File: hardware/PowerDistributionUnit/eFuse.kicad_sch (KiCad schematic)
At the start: 19 parts, among them Q2 NMOS, U1 TPS25983, U2 AD5258

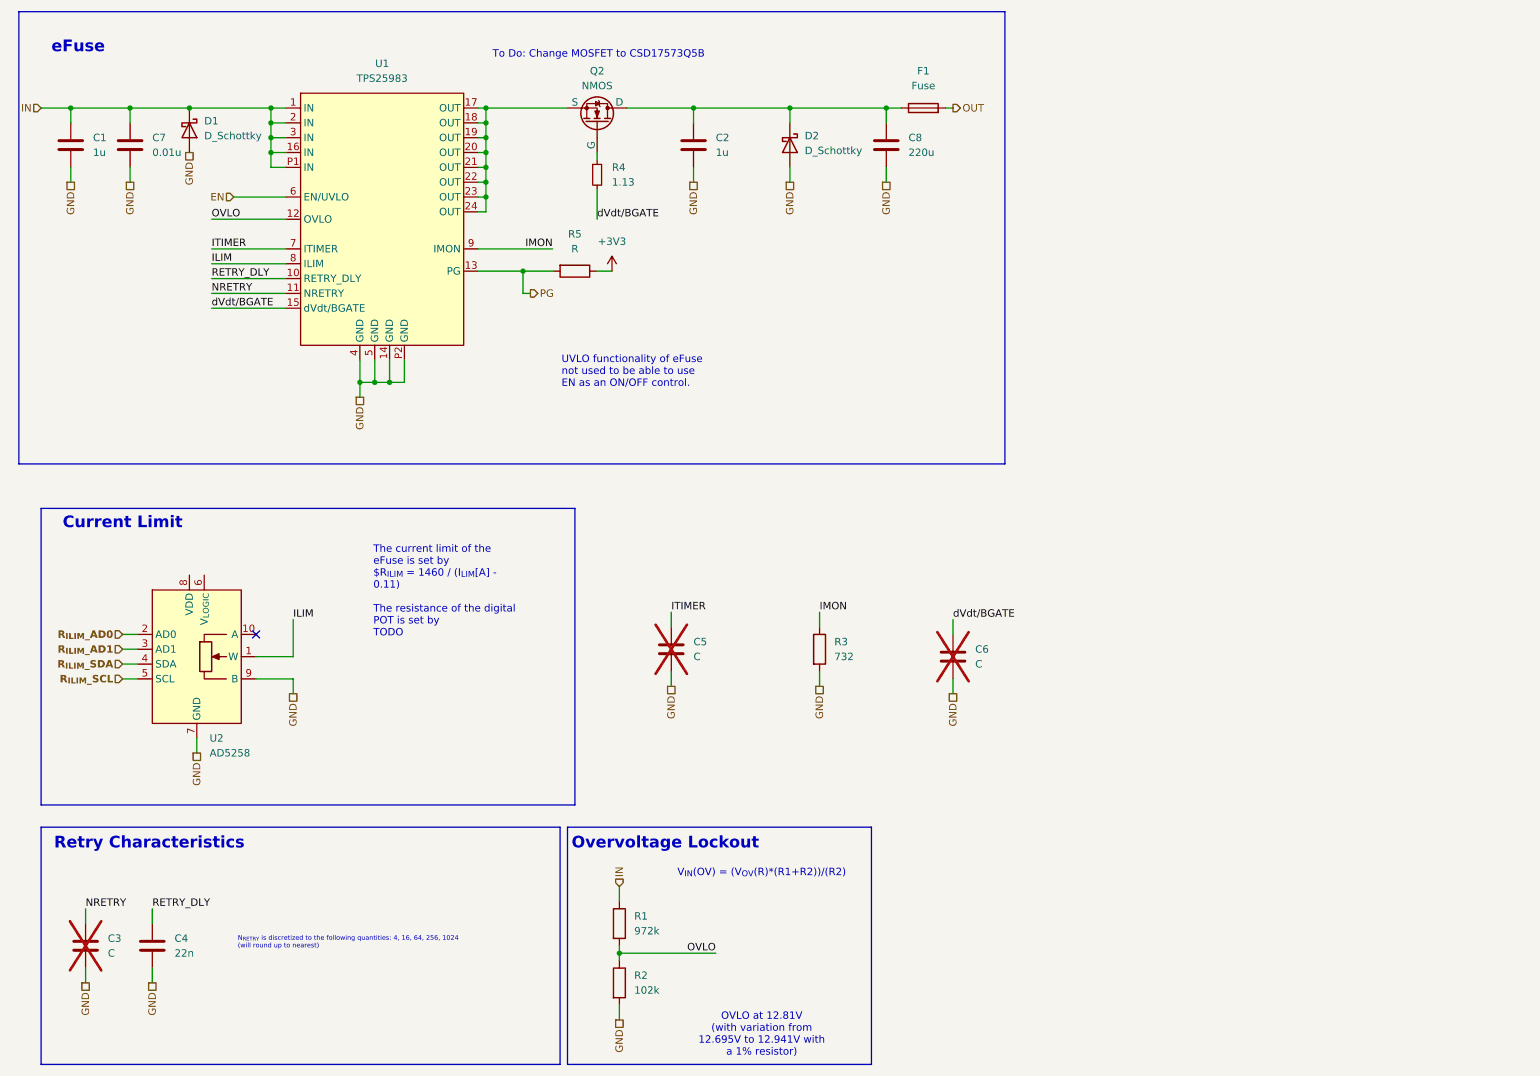
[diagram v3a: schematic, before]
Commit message: updated rev-i mosfet, organized parts, rearranged pins on digital pot symbol, added bypass caps, some rearranging, etc.
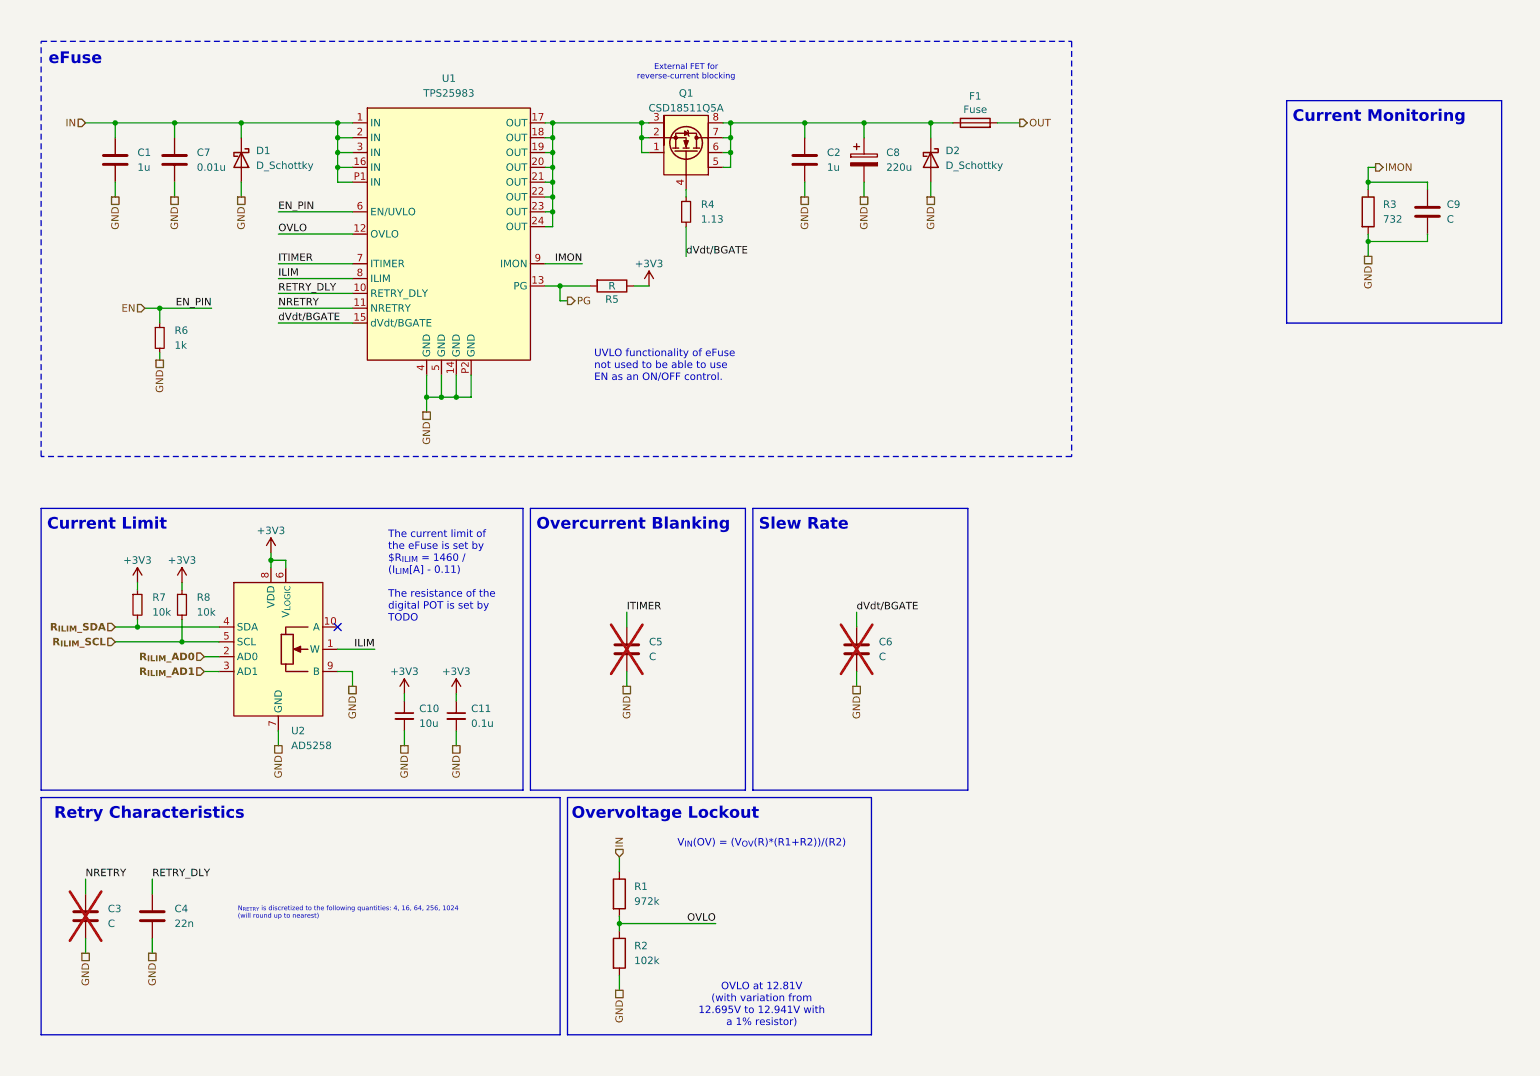
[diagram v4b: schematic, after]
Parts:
- removed C8: 220u, symbol Device:C
- removed Q2: NMOS, symbol Simulation_SPICE:NMOS
- added C10: 10u, symbol Device:C_Small
- added C11: 0.1u, symbol Device:C_Small
- added C8: 220u, symbol Device:C_Polarized
- added C9: C, symbol Device:C
- added Q1: CSD18511Q5A, symbol PowerDistributionUnitLib:CSD18511Q5A
- added R6: 1k, symbol Device:R_Small
- added R7, R8: 10k, symbol Device:R_Small
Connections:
- net +3V3: now also U2.6 (V_{LOGIC}), U2.8 (VDD), C10.1, C11.1, R7.1, R8.1
- net EN: now also R6.1
- net GND: now also C10.2, C11.2, C8.2, C9.2, R6.2
- net IMON: now also C9.1
- net R_{ILIM}_SCL: now also R8.2
- net R_{ILIM}_SDA: now also R7.2
- net at R4.1: now also Q1.4
- net at C2.1, D2.1 (K), F1.1: now also C8.1, Q1.5, Q1.6, Q1.7, Q1.8
- net at U1.17 (OUT), U1.18 (OUT), U1.19 (OUT)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: now also Q1.1, Q1.2, Q1.3
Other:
- note added: "Current Monitoring"
- note added: "Overcurrent Blanking"
- note added: "Slew Rate"
- note removed: "To Do: Change MOSFET to CSD17573Q5B"
- moved on the sheet: C1, C2, C3, C4, C5, C6, C7, D1, D2, F1, R1, R2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

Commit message: Finished eFuse schematic and now connecting everything
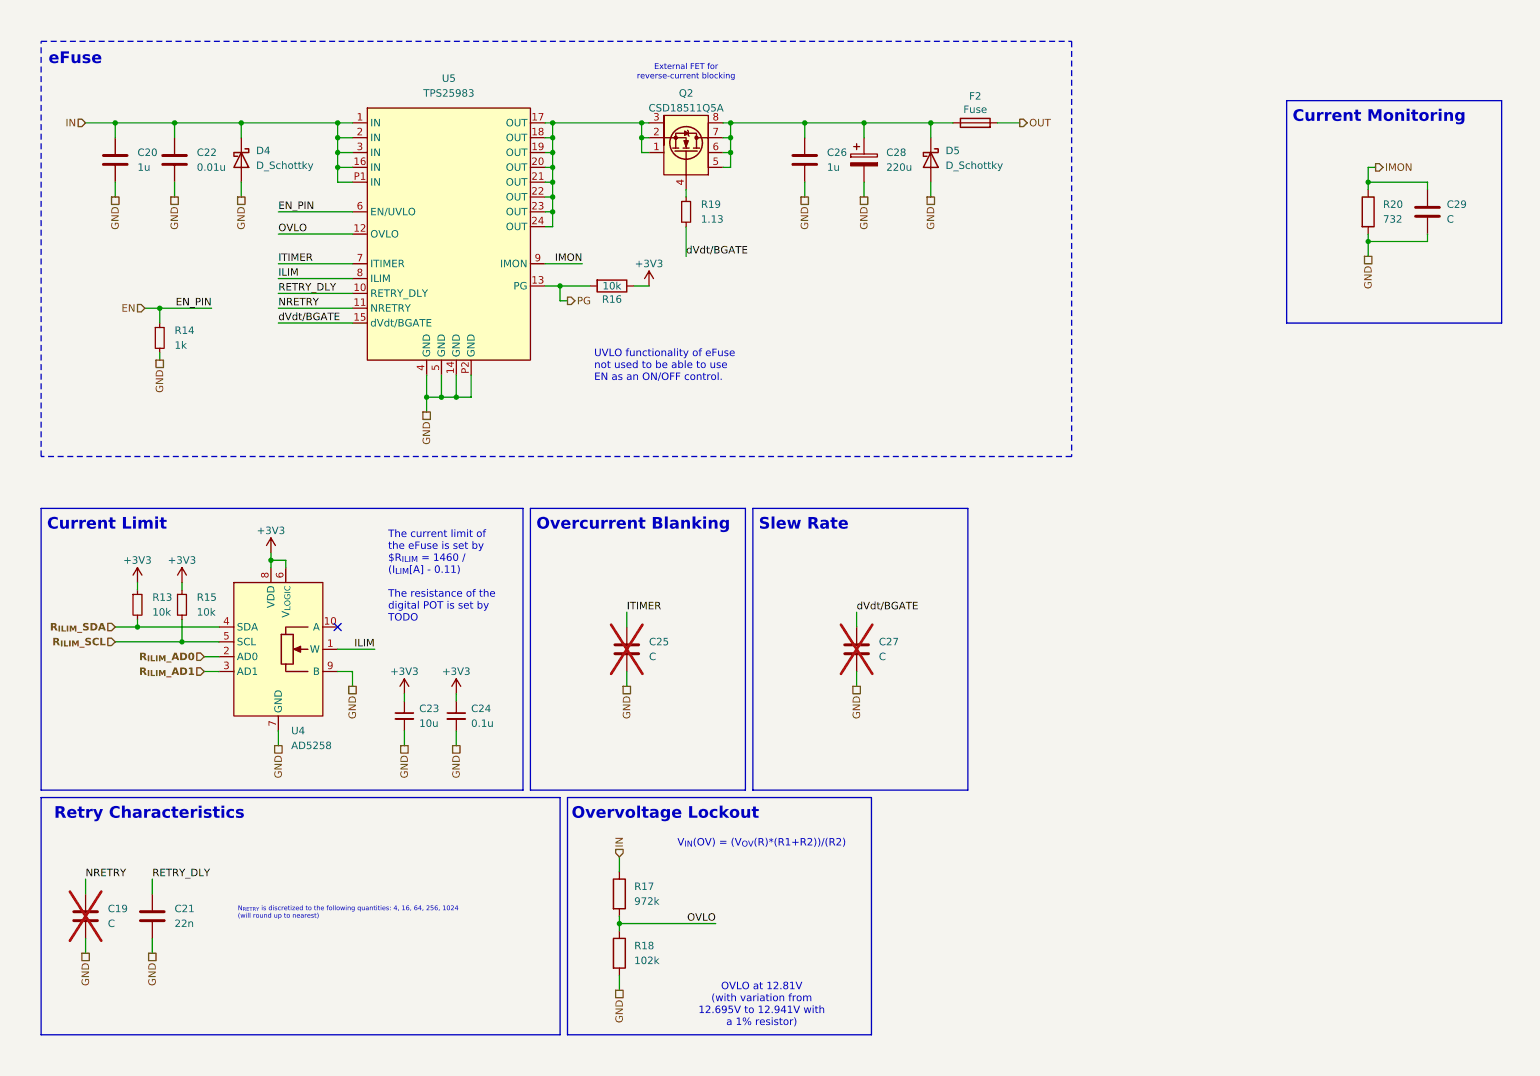
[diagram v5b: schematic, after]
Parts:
- R16: renamed from R5; value R -> 10k
- renumbered C3 to C19, C1 to C20, C4 to C21, C7 to C22, C10 to C23, C11 to C24, C5 to C25, C2 to C26, C6 to C27, C8 to C28, C9 to C29, D1 to D4, D2 to D5, F1 to F2, Q1 to Q2, R7 to R13, R6 to R14, R8 to R15, R1 to R17, R2 to R18, R4 to R19, R3 to R20, U2 to U4, U1 to U5

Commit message: split off monitoring to its own sheet, continued connecting hardware and adding symbols
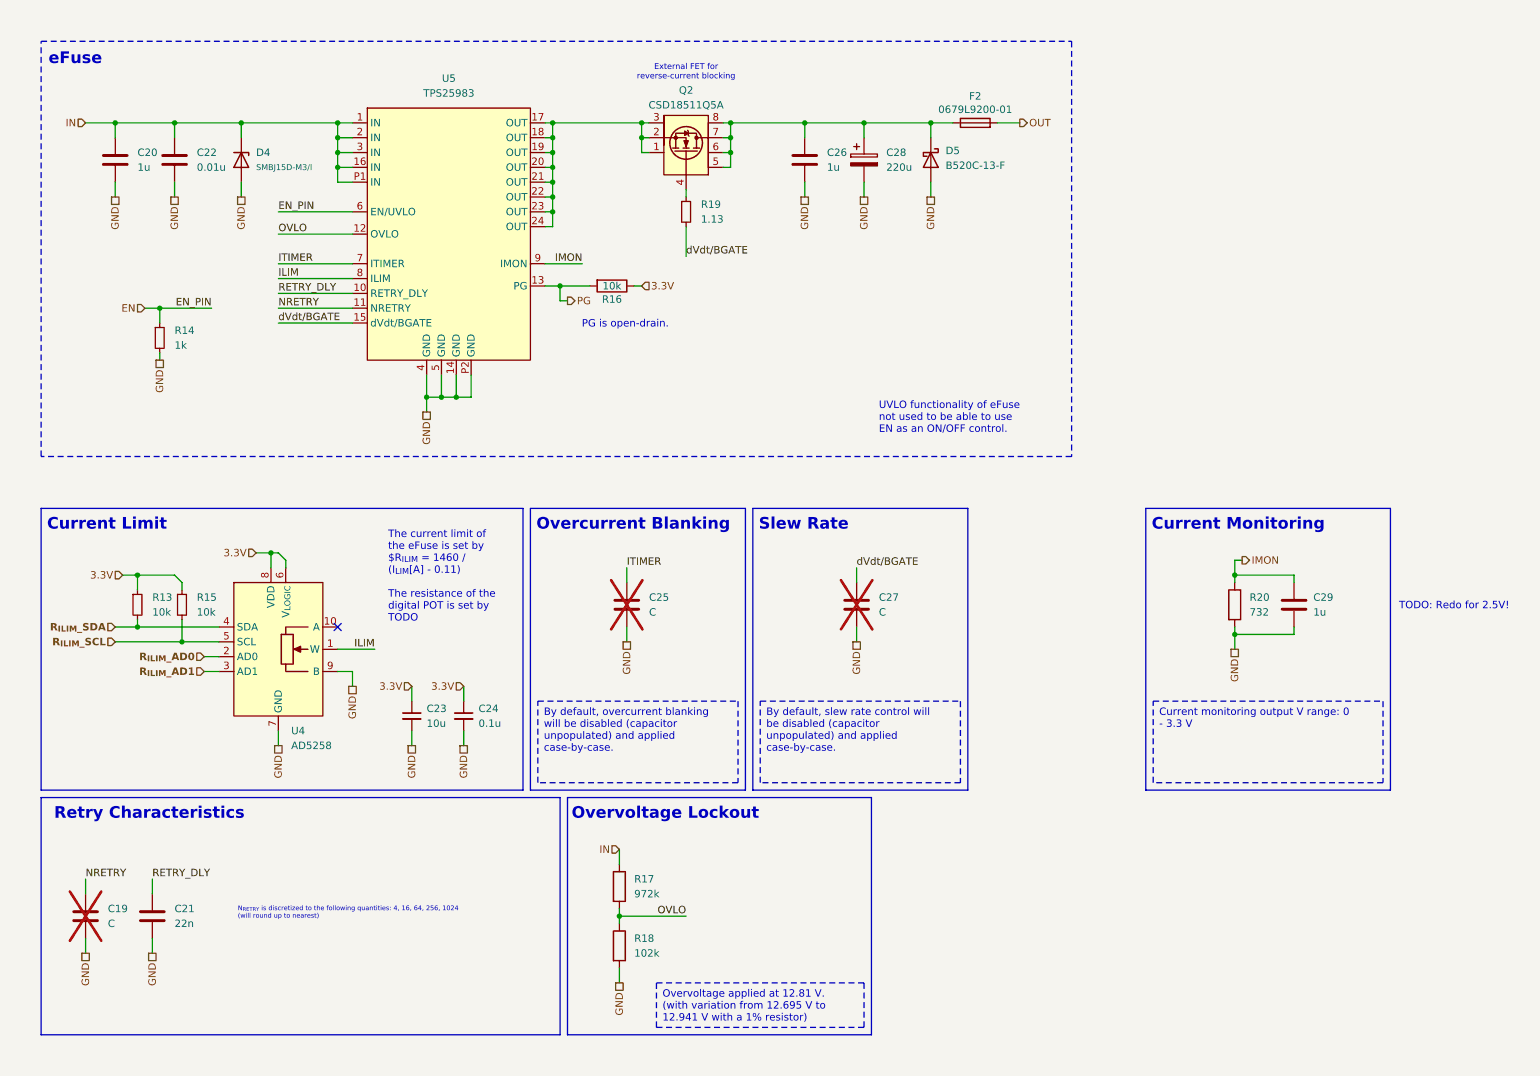
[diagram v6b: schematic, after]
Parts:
- C29: value C -> 1u
- D4: value D_Schottky -> SMBJ15D-M3/I; footprint (none) -> Diode_SMD:D_SMB; symbol Device:D_Schottky -> Device:D_Zener
- D5: value D_Schottky -> B520C-13-F; footprint (none) -> Diode_SMD:D_SMC
- F2: value Fuse -> 0679L9200-01
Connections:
- net +3V3 renamed 3.3V
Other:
- note added: "PG is open-drain."
- note added: "TODO: Redo for 2.5V!"
- note removed: "OVLO at 12.81V (with variation from 12.695V to 12.941V with a 1% resistor)"
- note removed: "V_{IN}(OV) = (V_{OV}(R)*(R1+R2))/(R2)"
- moved on the sheet: C23, C24, C25, C27, C29, R17, R18, R20

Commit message: added datasheets and footprints to PowerDistributionUnitLib symbol library
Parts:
- Q2: footprint (none) -> Package_SON:VSONP-8-1EP_5x6_P1.27mm
- U4: footprint (none) -> Package_SO:MSOP-10_3x3mm_P0.5mm
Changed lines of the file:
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@@
 			)
 		)
-		(property "Footprint" ""
+		(property "Footprint" "Package_SO:MSOP-10_3x3mm_P0.5mm"
 			(at 73.66 140.97 0)
 			(effects
@@
 			)
 		)
-		(property "Datasheet" ""
+		(property "Datasheet" "${KIPRJMOD}/lib/docs/AD5258.pdf"
 			(at 73.66 140.97 0)
 			(effects
@@
 			)
 		)
-		(property "Footprint" ""
+		(property "Footprint" "Package_SON:VSONP-8-1EP_5x6_P1.27mm"
 			(at 128.27 39.37 0)
 			(effects
@@
 			)
 		)
-		(property "Datasheet" ""
+		(property "Datasheet" "${KIPRJMOD}/lib/docs/csd18511q5a.pdf"
 			(at 128.27 39.37 0)
 			(effects
@@
 			)
 		)
-		(property "Datasheet" ""
+		(property "Datasheet" "${KIPRJMOD}/lib/docs/tps25983.pdf"
 			(at 80.01 35.56 0)
 			(effects
